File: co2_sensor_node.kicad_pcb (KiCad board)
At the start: 4 copper layers, 77.5 x 100 mm, 147 parts, among them J1 Conn_01x02, J10 Conn_01x02, J11 TF-15x15, J2 Conn_01x02, J3 Conn_01x03, J4 Conn_01x03, J5 Conn_01x02, J6 Conn_01x02, J7 Conn_01x04, J8 Conn_01x04, J9 Conn_01x04_Male, Q1 AO3400A, Q2 AO3401A, Q3 AO3401A, Q4 SS8050, Q5 SS8050, Q6 AO3400A, SW1 K2-1102SP-C4SC-04, U1 TPS55340PWP, U2 BQ24074RGT, U3 TPS62130, U4 CH340C, U5 ESP32-WROOM-32D, U6 TC1508S

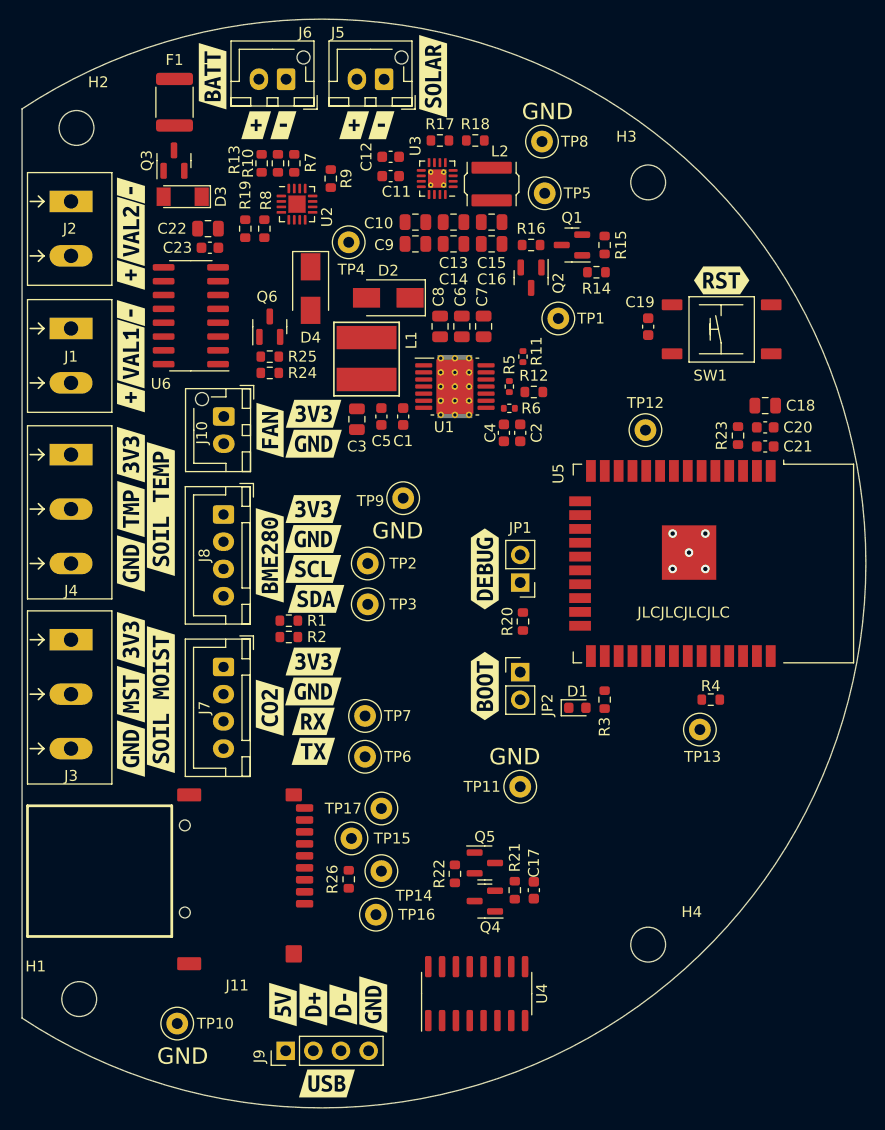
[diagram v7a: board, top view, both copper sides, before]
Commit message: Finish routing PCB revision 2
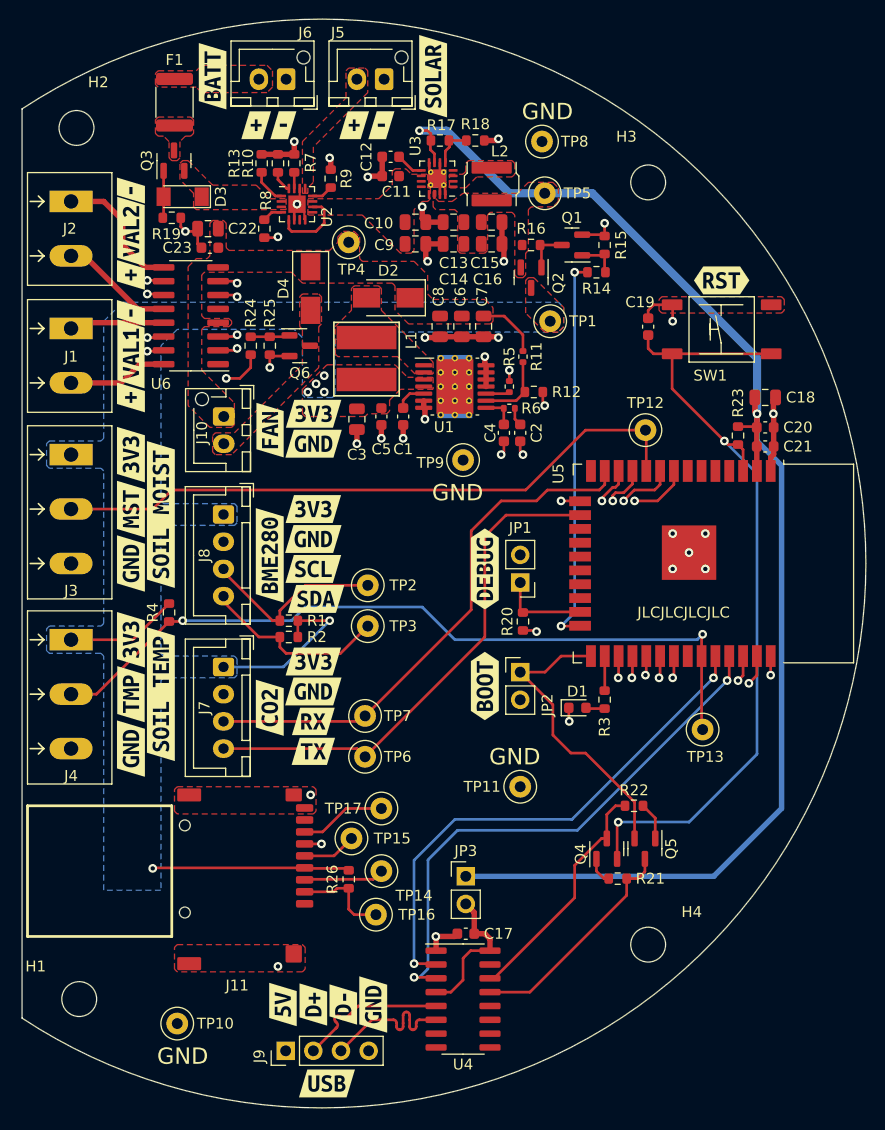
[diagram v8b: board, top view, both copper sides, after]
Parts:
- removed kibuzzard-629F6579: G***, kibuzzard-629F6579
- removed kibuzzard-629F66E0: G***, kibuzzard-629F66E0
- added JP3: USB_PWR_JP, Connector_PinHeader_2.54mm:PinHeader_1x02_P2.54mm_Vertical, F.Cu at (163.8, 133.7)
- added kibuzzard-62E4018B: G***, kibuzzard-62E4018B, B.Cu at (132.5, 97.6)
- added kibuzzard-62E4020F: G***, kibuzzard-62E4020F, B.Cu at (160.7, 114.0)
- moved R4 50.4 mm to (136.5, 109.5), turned to -90 degrees
- moved R22 17.6 mm to (179.2, 127.2), turned to 0 degrees
- moved J3 17.0 mm to (127.5, 95.0)
- moved J4 17.0 mm to (127.5, 112.0)
- moved kibuzzard-628CFF95 17.0 mm to (133.0, 112.0)
- moved kibuzzard-628CFF9F 17.0 mm to (133.0, 95.0)
- moved kibuzzard-628CFFA6 17.0 mm to (133.0, 122.0)
- moved kibuzzard-628CFFAE 17.0 mm to (133.0, 105.0)
- moved kibuzzard-628CFFC0 17.0 mm to (133.0, 117.0)
- moved kibuzzard-628CFFCE 17.0 mm to (133.0, 100.0)
- moved kibuzzard-628D086F 17.0 mm to (135.8, 117.0)
- moved kibuzzard-628D087A 17.0 mm to (135.8, 100.5)
- moved kibuzzard-629F65FE 15.9 mm to (157.1, 142.8)
- moved Q5 14.8 mm to (180.2, 131.2), turned to -90 degrees
- moved Q4 12.2 mm to (176.7, 131.2), turned to 90 degrees
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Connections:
- C17 pad 1: +3V3 -> Net-(JP3-Pad2)
- U4 pad 16: +3V3 -> Net-(JP3-Pad2)
- U4 pad 4: +3V3 -> Net-(JP3-Pad2)
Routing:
- net +3V3: track 0.07 -> 153.6 mm, vias 0 -> 2
- net GND: track 0.00 -> 92.4 mm, vias 5 -> 42
- net /Microprocessor section/EN: track 0.00 -> 75.7 mm, vias 0 -> 2
- net /Microprocessor section/TEMP_SENSOR: track 0.00 -> 71.6 mm, vias 0 -> 2
- net /Fan/FAN: track 0.00 -> 59.9 mm, vias 0 -> 2
- net /Microprocessor section/MOISTURE_SENSOR: track 0.00 -> 59.5 mm
- net /Microprocessor section/SPI_SD_CSN: track 0.00 -> 59.2 mm, vias 0 -> 1
- net /Microprocessor section/VALVE_1_FWD: track 0.00 -> 55.3 mm, vias 0 -> 2
- net /Microprocessor section/VALVE_1_REV: track 0.00 -> 53.8 mm, vias 0 -> 2
- net /Microprocessor section/VALVE_2_FWD: track 0.00 -> 53.4 mm, vias 0 -> 2
- net /Microprocessor section/VALVE_2_REV: track 0.00 -> 51.8 mm, vias 0 -> 2
- net /Microprocessor section/SPI_MOSI: track 0.00 -> 51.5 mm, vias 0 -> 1
- net /Microprocessor section/TXD0: track 0.00 -> 50.3 mm, vias 0 -> 2
- net /CO2 Sensor Connector/UART_RX: track 0.00 -> 49.5 mm
- net /Microprocessor section/RXD0: track 0.00 -> 48.1 mm, vias 0 -> 2
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- added copper zone on F.Cu, net +3V3
- added copper zone on F.Cu, net +5V
- added copper zone on F.Cu, net +BATT
- added copper zone on B.Cu, net /Power/3V3_switch
- added copper zone on F.Cu, net /Power/3V3_switch
- added copper zone on F.Cu, net /Power/PWR_OUT
- added copper zone on F.Cu, net GND
- added copper zone on F.Cu, net Net-(D2-Pad2)
- added copper zone on F.Cu, net Net-(D4-Pad2)
- added copper zone on F.Cu, net Net-(F1-Pad1)
- added copper zone on F.Cu, net Net-(F1-Pad2)
- added copper zone on F.Cu, net Net-(J5-Pad2)
- added copper zone on F.Cu, net Net-(L2-Pad1)
